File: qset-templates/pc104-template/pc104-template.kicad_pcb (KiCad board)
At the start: 2 copper layers, 8 parts

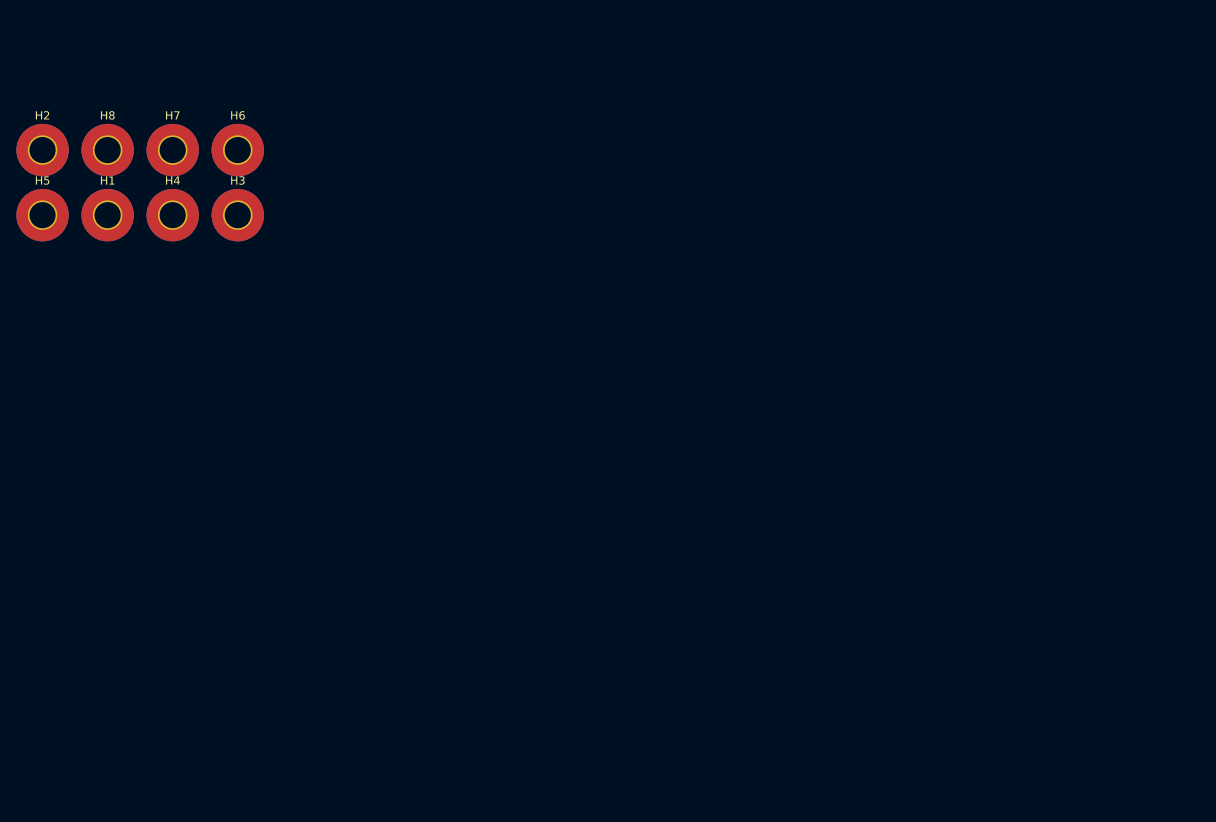
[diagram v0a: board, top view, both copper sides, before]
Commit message: templates: pc104: complete template with MH, PC104, and edges
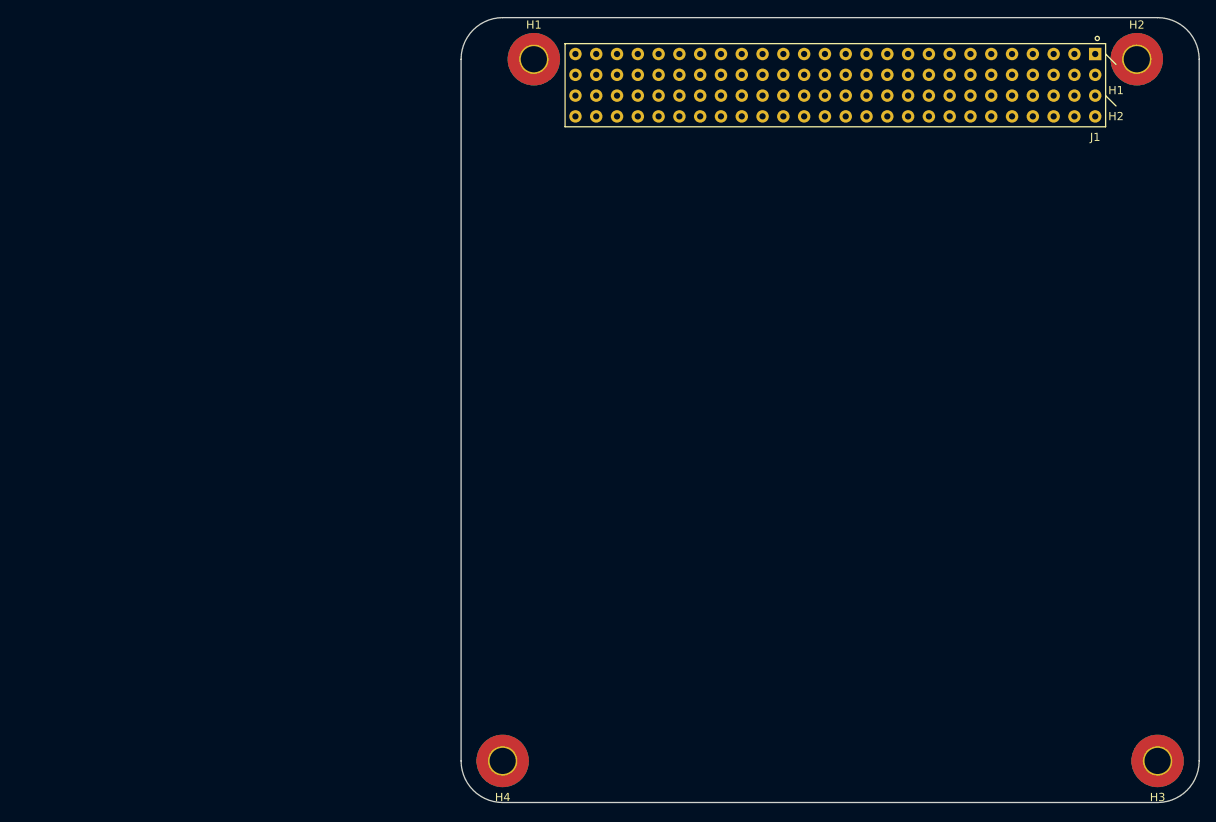
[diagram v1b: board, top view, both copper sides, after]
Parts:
- removed H5, H6, H7, H8: MountingHole_Pad, MountingHole:MountingHole_3.2mm_M3_Pad_TopBottom
- added J1: PC104_Connector, pc104-connector:pc104-connector, F.Cu at (156.2, 54.0)
- moved H2 134.1 mm to (191.8, 52.1)
- moved H3 130.7 mm to (194.3, 137.8)
- moved H4 77.9 mm to (114.3, 137.8)
- moved H1 55.4 mm to (118.1, 52.1)
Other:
- board outline added: 90.2 x 95.9 mm
- copper layers 2 -> 4

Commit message: templates: pc104: include cutouts on all 4 edges
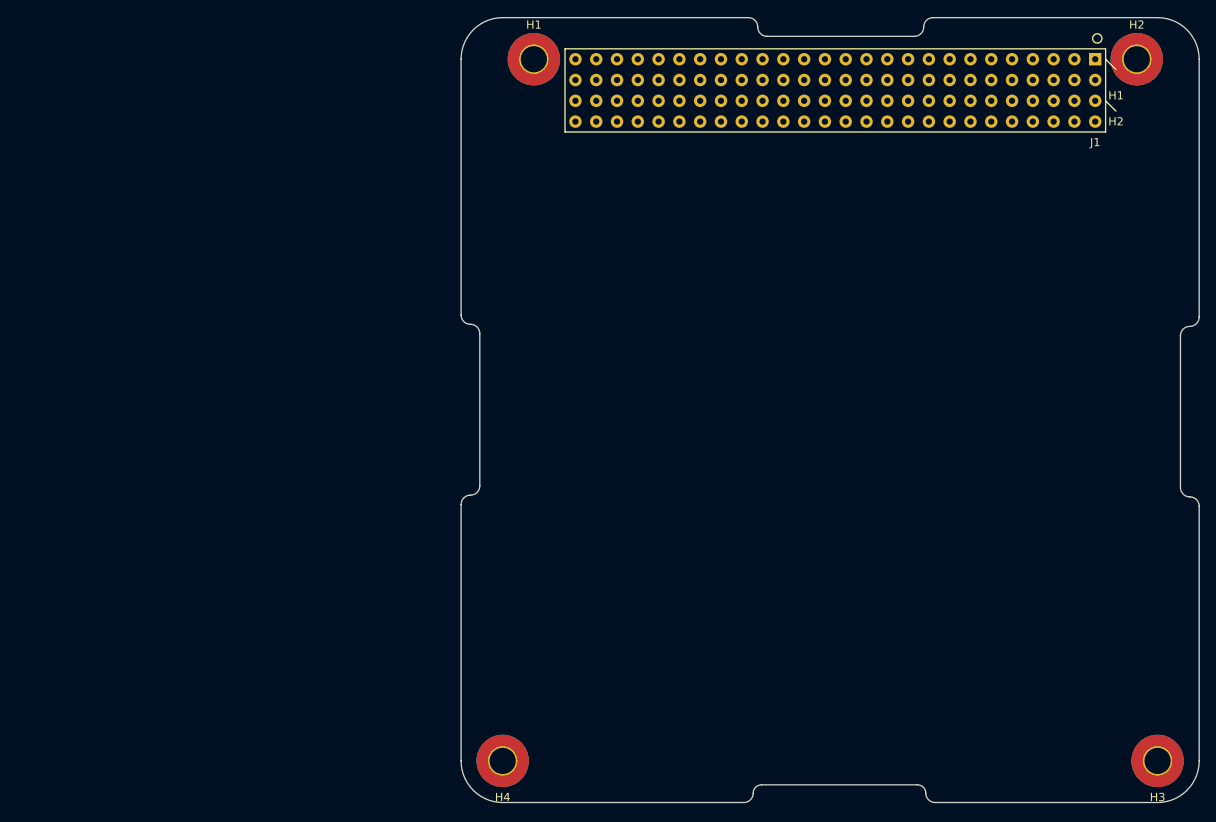
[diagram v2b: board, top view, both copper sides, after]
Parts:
- moved J1 0.63 mm to (156.2, 54.6)
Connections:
- J1 pad 54: (no net) -> unconnected-(J1-Pad54)
- J1 pad 56: (no net) -> unconnected-(J1-Pad56)
- J1 pad 58: (no net) -> unconnected-(J1-Pad58)
- J1 pad 60: (no net) -> unconnected-(J1-Pad60)
- J1 pad 62: (no net) -> unconnected-(J1-Pad62)
- J1 pad 64: (no net) -> unconnected-(J1-Pad64)
- J1 pad 66: (no net) -> unconnected-(J1-Pad66)
- J1 pad 68: (no net) -> unconnected-(J1-Pad68)
- J1 pad 70: (no net) -> unconnected-(J1-Pad70)
- J1 pad 72: (no net) -> unconnected-(J1-Pad72)
- J1 pad 74: (no net) -> unconnected-(J1-Pad74)
- J1 pad 76: (no net) -> unconnected-(J1-Pad76)
- J1 pad 78: (no net) -> unconnected-(J1-Pad78)
- J1 pad 80: (no net) -> unconnected-(J1-Pad80)
- J1 pad 82: (no net) -> unconnected-(J1-Pad82)
- J1 pad 84: (no net) -> unconnected-(J1-Pad84)
- J1 pad 86: (no net) -> unconnected-(J1-Pad86)
- J1 pad 88: (no net) -> unconnected-(J1-Pad88)
- J1 pad 90: (no net) -> unconnected-(J1-Pad90)
- J1 pad 92: (no net) -> unconnected-(J1-Pad92)
- J1 pad 94: (no net) -> unconnected-(J1-Pad94)
- J1 pad 96: (no net) -> unconnected-(J1-Pad96)
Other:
- outline, holes or cut-outs redrawn

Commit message: templates: pc104: remove material around MH locations, include step file for header connector
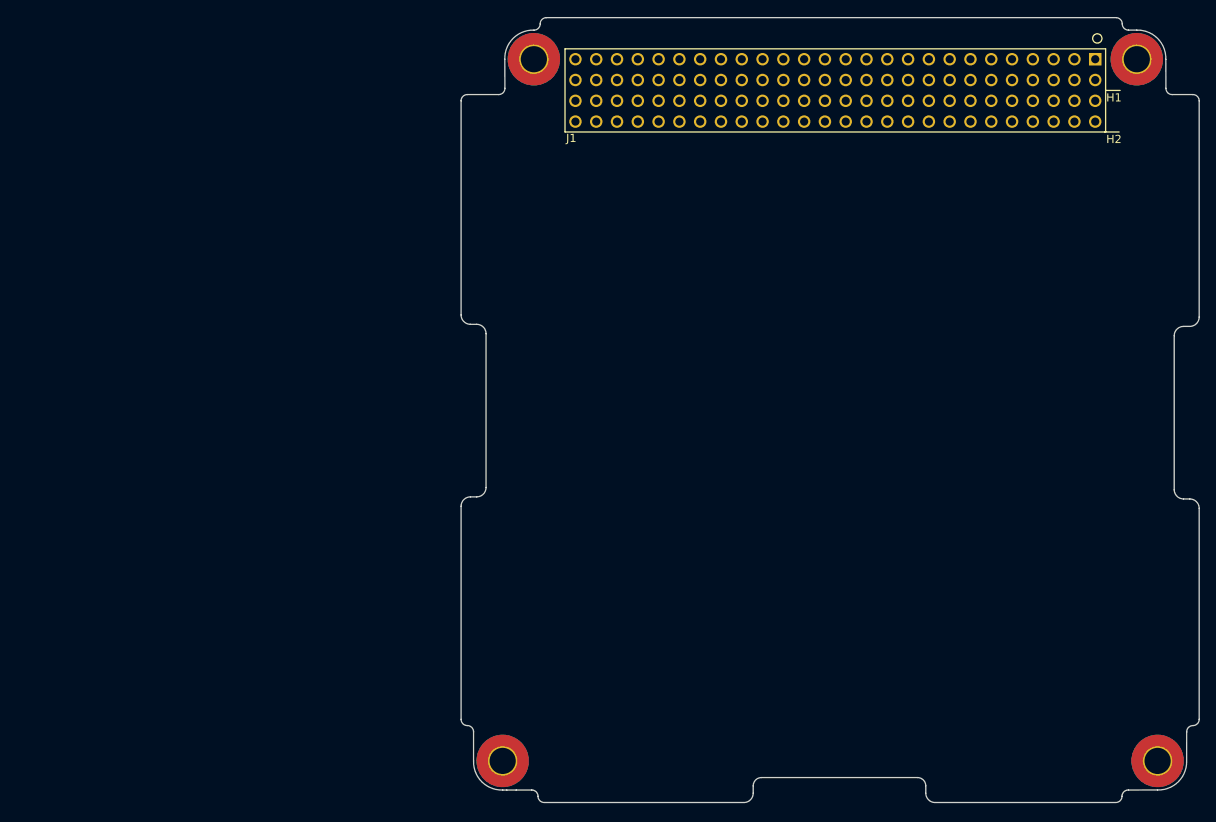
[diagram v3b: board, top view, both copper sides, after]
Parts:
- J1: footprint pc104-connector:pc104-connector -> pc104-template:pc104-connector
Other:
- outline, holes or cut-outs redrawn
